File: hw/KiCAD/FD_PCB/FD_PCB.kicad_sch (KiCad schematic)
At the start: 120 parts, among them J1 Barrel_Jack_Switch, J10 MQ-138 Gas Sensor, J11 KY-026 Flame Sensor, J12 MiCS-6814, J13 Conn_01x02, J14 HDC3022, J2 Conn_02x12_Odd_Even, J3 Conn_02x12_Odd_Even, J4 Conn_02x20_Odd_Even, J5 Conn_02x09_Odd_Even, J6 Conn_01x02, J7 Conn_02x09_Odd_Even, J8 MQ-4 Gas Sensor, J9 MQ-7 Gas Sensor, M1 Motor_Servo, M2 Motor_Servo, SW1 SW_Push, SW2 SW_Push, SW3 SW_Push, U1 Adafruit ST7735R, U2 MAX98357A, U3 ADS1115IDGS, U4 ADS1115IDGS, U5 Winsen ZE07-CO Module

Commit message: update kicad stuff
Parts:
- removed D5: Red LED, ECE445L:LED_D5.0mm, symbol ECE445L:LED
- removed D6: Green LED, ECE445L:LED_D5.0mm, symbol ECE445L:LED
- removed J5, J7: Conn_02x09_Odd_Even, symbol Connector_Generic:Conn_02x09_Odd_Even
- removed R3: 2k, symbol Device:R_US
- removed R4: 1k, symbol Device:R_US
- removed TP10: TestPoint, symbol Connector:TestPoint
- added J16, J7: Conn_01x08, symbol Connector_Generic:Conn_01x08
- added J5, J8: Conn_02x10_Odd_Even, symbol Connector_Generic:Conn_02x10_Odd_Even
- added TP1: TestPoint, symbol Connector:TestPoint
- renumbered J9 to J10, J10 to J11, J11 to J12, J12 to J13, J13 to J14, J14 to J15, J8 to J9, R12 to R10, R13 to R11, R14 to R12, R15 to R13, R16 to R14, R17 to R15, R18 to R16, R19 to R17, R20 to R18, R21 to R19, R22 to R20, R23 to R21, R24 to R22, R25 to R23, R26 to R24, R27 to R25, R28 to R26, R29 to R27, R30 to R28, R31 to R29, R5 to R3, R7 to R4, R9 to R5, R8 to R7, R10 to R8, R11 to R9, TP9 to TP10, TP15 to TP11, TP11 to TP12, TP12 to TP13, TP13 to TP14, TP7 to TP15, TP1 to TP2, TP2 to TP3, TP3 to TP4, TP4 to TP5, TP5 to TP6, TP6 to TP7, TP14 to TP8, TP8 to TP9
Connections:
- net +3V3: now also J2.5 (Pin_5), J5.7 (Pin_7), J5.9 (Pin_9); no longer D2.2 (A)
- net +5V: now also J5.1 (Pin_1), J5.3 (Pin_3), J5.5 (Pin_5); no longer D1.2 (A)
- net GND: now also J5.10 (Pin_10), J5.12 (Pin_12), J5.14 (Pin_14), J5.16 (Pin_16), J5.18 (Pin_18), J5.2 (Pin_2), J5.20 (Pin_20), J5.4 (Pin_4), J5.6 (Pin_6), J5.8 (Pin_8)
- net GPIO01: now also J2.15 (Pin_15); no longer J2.13 (Pin_13)
- net GPIO09: now also J2.19 (Pin_19); no longer J2.17 (Pin_17)
- net GPIO11: now also J2.17 (Pin_17); no longer J2.15 (Pin_15)
- net GPIO12: now also J5.19 (Pin_19); no longer J2.23 (Pin_23)
- net I2C1_SCL: now also J5.15 (Pin_15)
- net I2C1_SDA: now also J5.17 (Pin_17)
- net SB_+3V3: now also R7.1, J7.3 (Pin_3), J8.7 (Pin_7), J8.9 (Pin_9)
- net SB_+5V: now also J7.1 (Pin_1), J8.1 (Pin_1), J8.3 (Pin_3), J8.5 (Pin_5)
- net SB_GND: now also R6.1, J8.10 (Pin_10), J8.12 (Pin_12), J8.14 (Pin_14), J8.16 (Pin_16), J8.18 (Pin_18), J8.2 (Pin_2), J8.20 (Pin_20), J8.4 (Pin_4), J8.6 (Pin_6), J8.8 (Pin_8)
- net SB_I2C1_SCL: now also J8.15 (Pin_15)
- net SB_I2C1_SDA: now also J8.17 (Pin_17)
- net SB_UART1_RXD: now also J8.13 (Pin_13)
- net SB_UART1_TXD: now also J8.11 (Pin_11)
- net SPI0_CS0: now also J2.13 (Pin_13); no longer J2.11 (Pin_11)
- net SPI0_MISO: now also J2.9 (Pin_9); no longer J2.7 (Pin_7)
- net SPI0_MOSI: now also J2.11 (Pin_11); no longer J2.9 (Pin_9)
- net SPI0_SCK: now also J2.7 (Pin_7); no longer J2.5 (Pin_5)
- net SPI1_CS1: now also J2.23 (Pin_23); no longer J2.19 (Pin_19)
- net UART1_RXD: now also J5.13 (Pin_13)
- net UART1_TXD: now also J5.11 (Pin_11)
- net UI_+3V3: now also J3.5 (Pin_5), TP1.1; no longer R7.1
- net UI_GND: no longer R6.1
- net UI_GPIO01: now also J3.15 (Pin_15); no longer J3.13 (Pin_13)
- net UI_GPIO09: now also J3.19 (Pin_19); no longer J3.17 (Pin_17)
- net UI_GPIO11: now also J3.17 (Pin_17); no longer J3.15 (Pin_15)
- net UI_SPI0_CS0: now also J3.13 (Pin_13); no longer J3.11 (Pin_11)
- net UI_SPI0_MISO: now also J3.9 (Pin_9); no longer J3.7 (Pin_7)
- net UI_SPI0_MOSI: now also J3.11 (Pin_11); no longer J3.9 (Pin_9)
- net UI_SPI0_SCK: now also J3.7 (Pin_7); no longer J3.5 (Pin_5)
- net UI_SPI1_CS1: now also J3.23 (Pin_23), TP3.1; no longer J3.19 (Pin_19), TP15.1
- net LED_RED-: now reaches R8.2
- net LED_RED-: now also J7.2 (Pin_2)
- net at D2.1 (K): now also J16.4 (Pin_4)
- net LED_GREEN-: now reaches R9.2
- net LED_GREEN-: now also J7.4 (Pin_4)
- net at D4.1 (K): now also J16.8 (Pin_8); no longer R6.2
- net at D1.1 (K): now also J16.2 (Pin_2)
- net at D3.2 (A): now also J16.5 (Pin_5); no longer R7.2
- removed net UI_GPIO12: D3.1 (K), D4.2 (A), J3.23 (Pin_23), TP3.1
- new net: D1.2 (A), J16.1 (Pin_1)
- new net: D4.2 (A), J16.7 (Pin_7)
- new net: D2.2 (A), J16.3 (Pin_3)
- new net: D3.1 (K), J16.6 (Pin_6)
- new net LED_BLUE+: J7.5 (Pin_5), R7.2
- new net LED_BLUE-: J7.6 (Pin_6), J7.7 (Pin_7), J8.19 (Pin_19), TP15.1
- new net LED_YELLOW-: J7.8 (Pin_8), R6.2
- no-connect marks 28 -> 27
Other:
- note added: "20-Trace Ribbon Cable"
- note added: "LED BOARD"
- note added: "LED BOARD CONN"
- note removed: "18-Trace Ribbon Cable"
- moved on the sheet: R5, R6, R7, R9, SW3, TP11, TP12, TP13, TP14, TP15, TP8

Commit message: Finish schematic and start on PCB design. Much progress.
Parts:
- removed C1, C2, C3, C4: C, ECE445L:C_Axial_200mil, symbol ECE445L:C
- removed FB1, FB2: FerriteBead, symbol Device:FerriteBead
- removed R3, R4: 100k, symbol Device:R_US
- removed TP11, TP6, TP7: TestPoint, symbol Connector:TestPoint
- removed U1: Adafruit ST7735R, ECE445L:adafruit_st7735r2, symbol ECE445L:Adafruit_ST7735R
- removed U2: MAX98357A, Package_DFN_QFN:TQFN-16-1EP_3x3mm_P0.5mm_EP1.23x1.23mm, symbol MichaelECEPartsCustom:MAX98357A-Modified
- removed U5: Winsen ZE07-CO Module, symbol MichaelECEPartsCustom:ZE07-CO
- added C1, C2, C3: 220u, ECE445L:CP_Radial_Tantal200mil, symbol ECE445L:C_Polarized
- added C10, C11, C12, C15: 1u, Capacitor_SMD:C_0805_2012Metric, symbol ECE445L:C
- added C16: 10u, ECE445L:C_Axial_200mil, symbol ECE445L:C
- added C17, C18, C19, C20: 0.1u, Capacitor_SMD:C_0805_2012Metric, symbol ECE445L:C
- added C21, C4, C5: 4.7u, ECE445L:CP_Radial_Tantal200mil, symbol ECE445L:C_Polarized
- added C6, C9: 47u, ECE445L:CP_Radial_Tantal200mil, symbol ECE445L:C_Polarized
- added D5: +5V PWR, ECE445L:LED_D5.0mm, symbol ECE445L:LED
- added D6: +3V3 PWR, ECE445L:LED_D5.0mm, symbol ECE445L:LED
- added J10, J11, J7: Conn_01x02, Connector_PinHeader_2.54mm:PinHeader_1x02_P2.54mm_Vertical, symbol Connector_Generic:Conn_01x02
- added J18: Conn_01x10, Connector_PinHeader_2.00mm:PinHeader_1x10_P2.00mm_Vertical, symbol Connector_Generic:Conn_01x10
- added J19: Conn_01x05, Connector_PinHeader_2.00mm:PinHeader_1x05_P2.00mm_Vertical, symbol Connector_Generic:Conn_01x05
- added J6: Conn_01x07, Connector_PinHeader_2.54mm:PinHeader_1x07_P2.54mm_Vertical, symbol Connector_Generic:Conn_01x07
- added J9: Conn_01x16, Connector_PinHeader_2.54mm:PinHeader_1x16_P2.54mm_Vertical, symbol Connector_Generic:Conn_01x16
- added R19: 560k, Resistor_SMD:R_0805_2012Metric, symbol Device:R_US
- added R2: 100k, Resistor_SMD:R_0805_2012Metric, symbol Device:R_US
- added R20: 150k, Resistor_SMD:R_0805_2012Metric, symbol Device:R_US
- added R21: 15k, Resistor_SMD:R_0805_2012Metric, symbol Device:R_US
- added R32, R33: 0, Resistor_SMD:R_0805_2012Metric, symbol Device:R_US
- added R34: 2k, Resistor_SMD:R_0805_2012Metric, symbol Device:R_US
- added R35: 1k, Resistor_SMD:R_0805_2012Metric, symbol Device:R_US
- added TP46, TP5, TP8: TestPoint, TestPoint:TestPoint_Loop_D3.50mm_Drill1.4mm_Beaded, symbol Connector:TestPoint
- added U2, U3: OPA2350, ECE445L:DIP-8_W7.62mm_LongPads, symbol ECE445L:OPA2350
- C13: renamed from C6; footprint ECE445L:C_Axial_200mil -> Capacitor_SMD:C_0805_2012Metric
- C14: renamed from C8; footprint ECE445L:C_Axial_200mil -> Capacitor_SMD:C_0805_2012Metric
- C7: renamed from C5; footprint ECE445L:C_Axial_200mil -> Capacitor_SMD:C_0805_2012Metric
- C8: renamed from C7; footprint ECE445L:C_Axial_200mil -> Capacitor_SMD:C_0805_2012Metric
- FB1: renamed from FB3; footprint (none) -> Resistor_SMD:R_0603_1608Metric
- FB2: renamed from FB5; footprint (none) -> Resistor_SMD:R_0603_1608Metric
- FB3: renamed from FB4; footprint (none) -> Resistor_SMD:R_0603_1608Metric
- FB4: renamed from FB6; footprint (none) -> Resistor_SMD:R_0603_1608Metric
- J1: footprint (none) -> Connector_BarrelJack:BarrelJack_Wuerth_6941xx301002
- J12: renamed from J6; footprint (none) -> Connector_JST:JST_PH_B2B-PH-K_1x02_P2.00mm_Vertical
- J13: renamed from J8; footprint (none) -> Connector_PinHeader_2.54mm:PinHeader_2x10_P2.54mm_Vertical
- J14: renamed from J9; footprint (none) -> Connector_PinHeader_2.54mm:PinHeader_1x04_P2.54mm_Vertical
- J15: renamed from J10; footprint (none) -> Connector_PinHeader_2.54mm:PinHeader_1x04_P2.54mm_Vertical
- J16: renamed from J11; footprint (none) -> Connector_PinHeader_2.54mm:PinHeader_1x04_P2.54mm_Vertical
- J17: renamed from J12; footprint (none) -> Connector_PinHeader_2.54mm:PinHeader_1x04_P2.54mm_Vertical
- J2, J3: footprint (none) -> Connector_PinHeader_2.54mm:PinHeader_2x12_P2.54mm_Vertical
- J20: renamed from J15; footprint (none) -> Connector_PinHeader_2.54mm:PinHeader_1x06_P2.54mm_Vertical
- J21: renamed from J16; footprint (none) -> Connector_PinHeader_2.54mm:PinHeader_1x08_P2.54mm_Vertical
- J22: renamed from J13; footprint (none) -> Connector_PinHeader_2.54mm:PinHeader_1x05_P2.54mm_Vertical
- J23: renamed from J14; footprint (none) -> Connector_PinHeader_2.54mm:PinHeader_1x02_P2.54mm_Vertical
- J4: footprint (none) -> Connector_PinHeader_2.54mm:PinHeader_2x20_P2.54mm_Vertical
- J5: footprint (none) -> Connector_PinHeader_2.54mm:PinHeader_2x10_P2.54mm_Vertical
- J8: renamed from J7; footprint (none) -> Connector_PinHeader_2.54mm:PinHeader_1x08_P2.54mm_Vertical
- M1, M2: footprint (none) -> Connector_PinHeader_2.54mm:PinHeader_1x03_P2.54mm_Vertical
- R1: footprint (none) -> Resistor_SMD:R_0805_2012Metric
- R10: renamed from R11; footprint (none) -> Resistor_SMD:R_0805_2012Metric
- R11: renamed from R12; footprint (none) -> Resistor_SMD:R_0805_2012Metric
- R12: renamed from R16; footprint (none) -> Resistor_SMD:R_0805_2012Metric
- R13: renamed from R17; footprint (none) -> Resistor_SMD:R_0805_2012Metric
- R14: renamed from R18; footprint (none) -> Resistor_SMD:R_0805_2012Metric
- R15: renamed from R22; footprint (none) -> Resistor_SMD:R_0805_2012Metric
- R16: renamed from R24; footprint (none) -> Resistor_SMD:R_0805_2012Metric
- R17: renamed from R26; footprint (none) -> Resistor_SMD:R_0805_2012Metric
- R18: renamed from R28; footprint (none) -> Resistor_SMD:R_0805_2012Metric
- R22: renamed from R13; footprint (none) -> Resistor_SMD:R_0805_2012Metric
- R23: renamed from R14; footprint (none) -> Resistor_SMD:R_0805_2012Metric
- R24: renamed from R15; footprint (none) -> Resistor_SMD:R_0805_2012Metric
- R25: renamed from R19; footprint (none) -> Resistor_SMD:R_0805_2012Metric
- R26: renamed from R20; footprint (none) -> Resistor_SMD:R_0805_2012Metric
- R27: renamed from R21; footprint (none) -> Resistor_SMD:R_0805_2012Metric
- R28: renamed from R23; footprint (none) -> Resistor_SMD:R_0805_2012Metric
- R29: renamed from R25; footprint (none) -> Resistor_SMD:R_0805_2012Metric
- R3: renamed from R2; footprint (none) -> Resistor_SMD:R_0805_2012Metric
- R30: renamed from R27; footprint (none) -> Resistor_SMD:R_0805_2012Metric
- R31: renamed from R29; footprint (none) -> Resistor_SMD:R_0805_2012Metric
- R4: renamed from R5; footprint (none) -> Resistor_SMD:R_0805_2012Metric
- R5: renamed from R6; footprint (none) -> Resistor_SMD:R_0805_2012Metric
- R6: renamed from R7; footprint (none) -> Resistor_SMD:R_0805_2012Metric
- R7: renamed from R8; footprint (none) -> Resistor_SMD:R_0805_2012Metric
- R8: renamed from R9; footprint (none) -> Resistor_SMD:R_0805_2012Metric
- R9: renamed from R10; footprint (none) -> Resistor_SMD:R_0805_2012Metric
- SW1, SW2, SW3: footprint (none) -> Button_Switch_THT:SW_PUSH_6mm
- TP1, TP10, TP12, TP13, TP14, TP15, TP16, TP17, TP18, TP19, TP2, TP20, TP21, TP22, TP23, TP24, TP25, TP26, TP27, TP28, TP29, TP3, TP30, TP31, TP32, TP33, TP34, TP35, TP36, TP37, TP38, TP39, TP4, TP40, TP41, TP42, TP45, TP9: footprint (none) -> TestPoint:TestPoint_Loop_D3.50mm_Drill1.4mm_Beaded
- TP43: renamed from TP44; footprint (none) -> TestPoint:TestPoint_Loop_D3.50mm_Drill1.4mm_Beaded
- TP44: renamed from TP43; footprint (none) -> TestPoint:TestPoint_Loop_D3.50mm_Drill1.4mm_Beaded
- TP6: renamed from TP5; footprint (none) -> TestPoint:TestPoint_Loop_D3.50mm_Drill1.4mm_Beaded
- TP7: renamed from TP8; footprint (none) -> TestPoint:TestPoint_Loop_D3.50mm_Drill1.4mm_Beaded
- renumbered U3 to U1
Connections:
- net +5V_EXT: now also C1.1, C16.1, C17.1, C18.1, C19.1, C2.1, C20.1, C3.1, C6.1, J10.1 (Pin_1), J6.1 (Pin_1), J7.1 (Pin_1)
- net Ain10: now also C10.1
- net Ain11: now also C11.1
- net Ain12: now also C12.1
- net GND: now also C1.2, C16.2, C17.2, C18.2, C19.2, C2.2, C20.2, C3.2, C6.2, J10.2 (Pin_2), J6.2 (Pin_2), J7.2 (Pin_2), R2.1, TP8.1
- net I2C1_SCL: now also J5.17 (Pin_17); no longer J5.15 (Pin_15)
- net I2C1_SDA: now also J5.15 (Pin_15); no longer J5.17 (Pin_17)
- net I2S0_DOUT: now also J6.5 (Pin_5)
- net I2S0_FS: now also J6.7 (Pin_7)
- net I2S0_SCK: now also J6.6 (Pin_6)
- net MiCS_CO: now also R24.2, U2.1, U2.2 (-); no longer J22.1 (Pin_1), R22.2
- net MiCS_NH3: now also U2.6 (-), U2.7; no longer J22.2 (Pin_2)
- net MiCS_NO2: now also R22.2, U3.1, U3.2 (-); no longer J22.3 (Pin_3), R24.2
- net SB_+3V3: now also C21.1, D6.2 (A)
- net SB_+5V: now also C15.2, C4.1, C5.1, C9.1, D5.2 (A), J18.1 (Pin_1), R19.1, R20.1, R21.1, U2.8 (V+), U3.8 (V+)
- net SB_GND: now also C10.2, C11.2, C12.2, C15.1, C21.2, C4.2, C5.2, C9.2, J18.2 (Pin_2), J19.5 (Pin_5), R33.1, R34.1, R35.1, U2.4 (V-), U3.4 (V-)
- net SB_I2C1_SCL: now also J13.17 (Pin_17); no longer J13.15 (Pin_15)
- net SB_I2C1_SDA: now also J13.15 (Pin_15); no longer J13.17 (Pin_17)
- net SB_UART1_RXD: now also J18.9 (Pin_9)
- net SB_UART1_TXD: now also J18.8 (Pin_8)
- net UI_+3V3: now also J9.15 (Pin_15), J9.2 (Pin_2)
- net UI_GND: now also TP9.1, J9.1 (Pin_1), J9.16 (Pin_16), TP46.1
- net UI_GPIO01: now also J9.6 (Pin_6)
- net UI_GPIO09: now also TP5.1
- net UI_GPIO11: now also J9.7 (Pin_7)
- net UI_SPI0_CS0: now also J9.10 (Pin_10)
- net UI_SPI0_MOSI: now also J9.8 (Pin_8)
- net UI_SPI0_SCK: now also J9.9 (Pin_9)
- net UI_SPI1_CS1: no longer TP9.1
- net ZE07-CO_DAC: now also J18.6 (Pin_6)
- net at J12.1 (Pin_1): now also J11.1 (Pin_1)
- net at J12.2 (Pin_2): now also J11.2 (Pin_2)
- new net: D5.1 (K), R34.2
- new net: J22.3 (Pin_3), R21.2, U3.3 (+)
- new net: J6.4 (Pin_4), R2.2
- new net: D6.1 (K), R35.2
- new net: J22.1 (Pin_1), R19.2, U2.3 (+)
- new net: J22.2 (Pin_2), R20.2, U2.5 (+)
- new net: R33.2, U3.5 (+)
- new net: R32.2, U3.6 (-)
- new net: R32.1, U3.7
- no-connect marks 27 -> 33
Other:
- note added: "MAX98357 Vout"
- note added: "MAX98357A Breakout"
- note added: "SEN0219 PWR"
- note added: "ST7735R LCD"
- note added: "Winsen ZE07-CO Module"
- moved on the sheet: C13, C14, FB3, FB4, J12, J22, J23, R22, R23, R24, R25, R26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

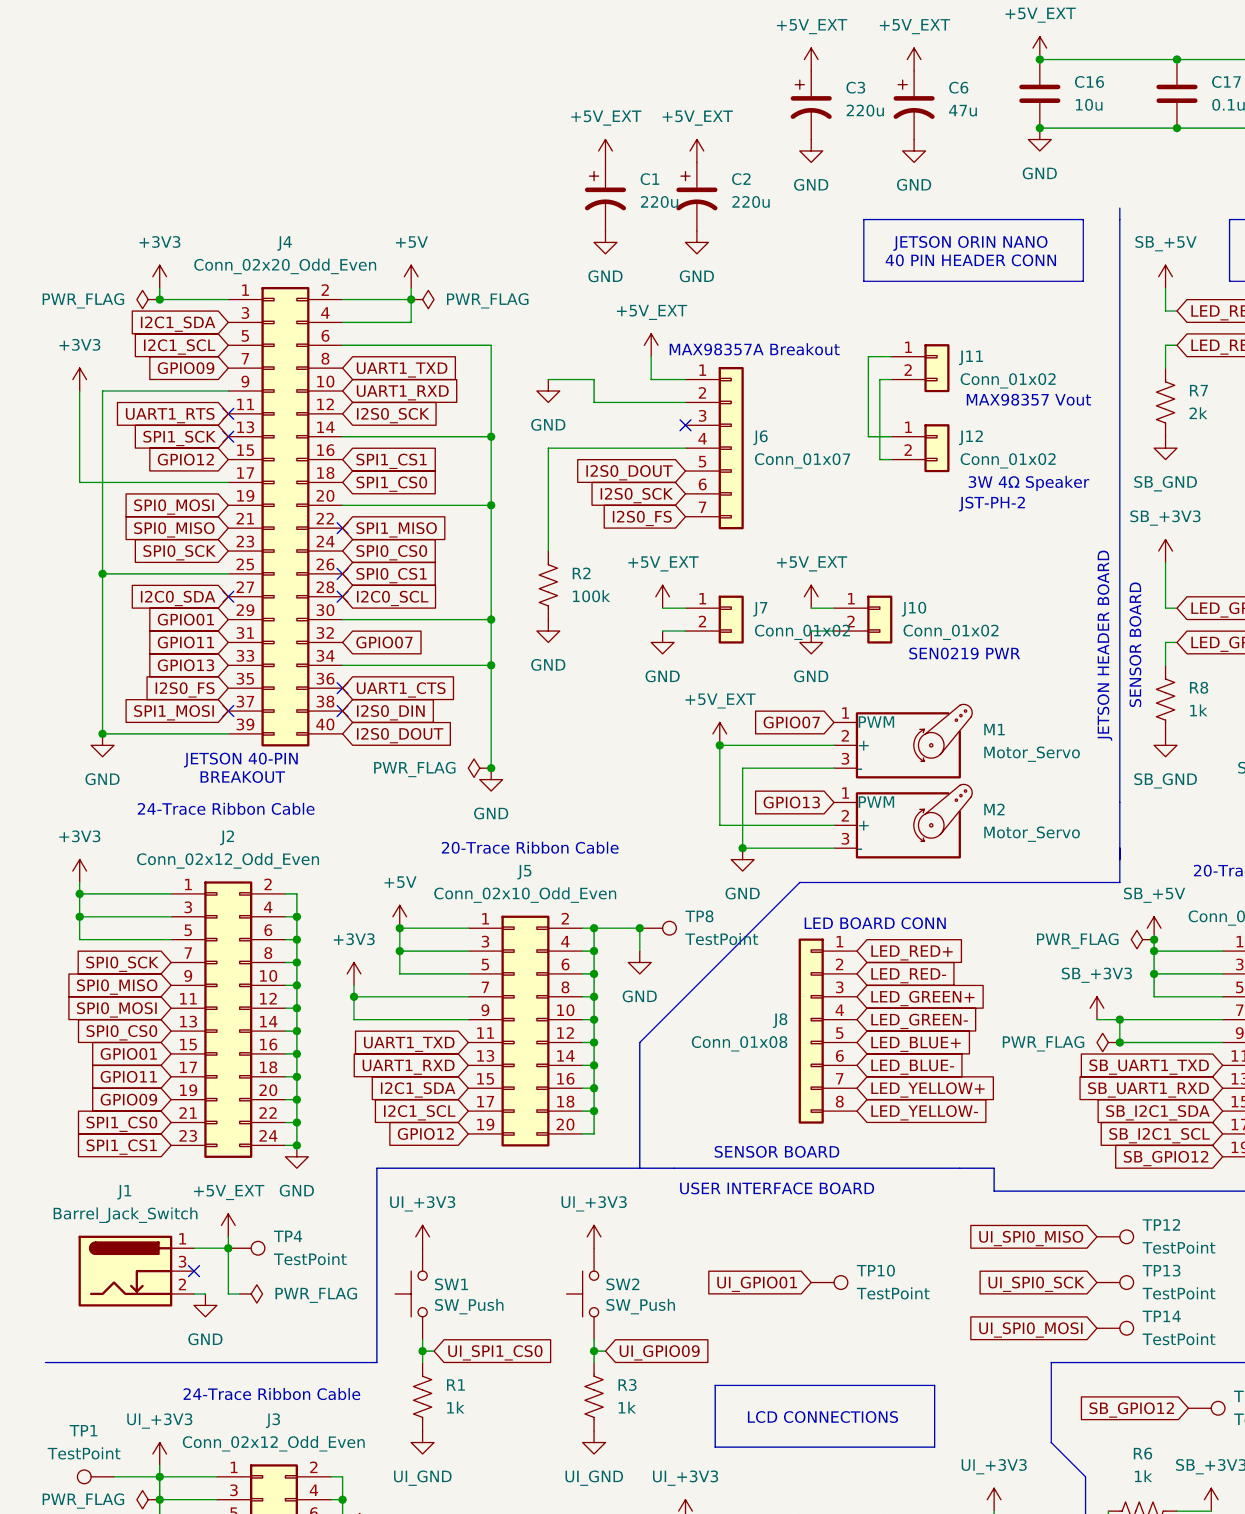
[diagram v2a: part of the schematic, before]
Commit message: finish sensor board, lcd board, led board, and header board
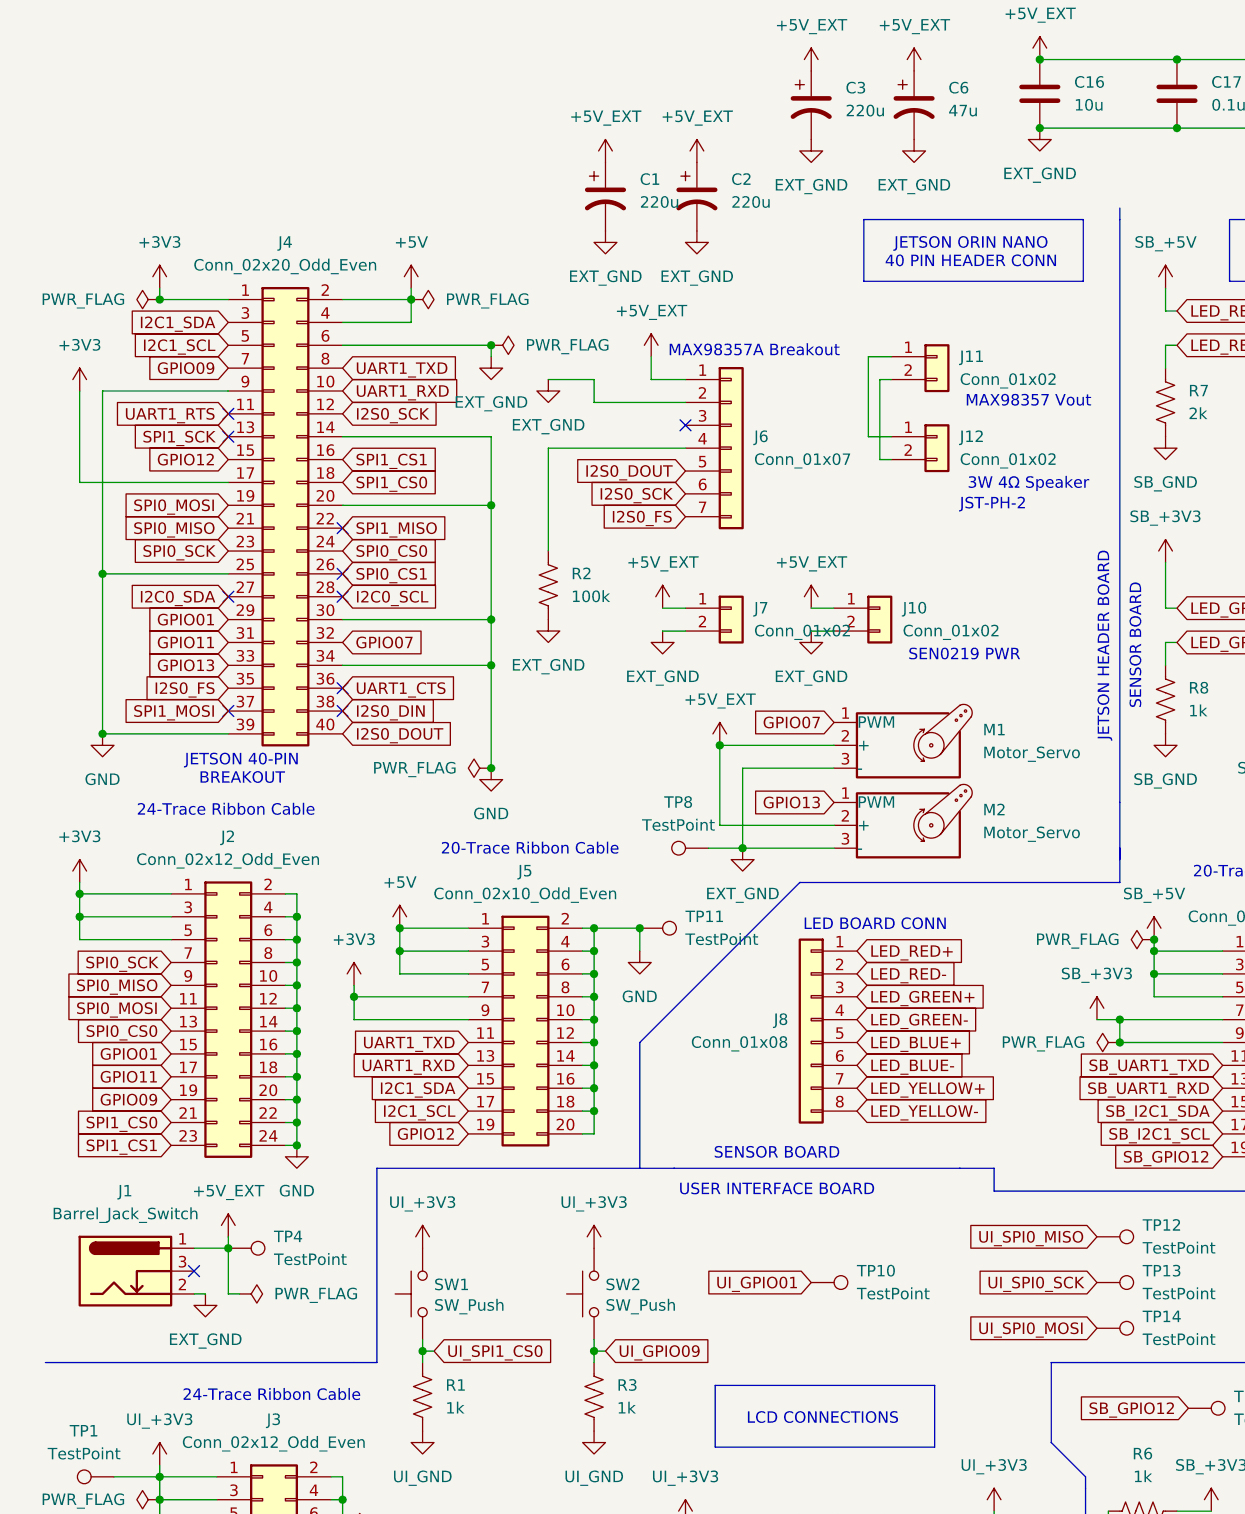
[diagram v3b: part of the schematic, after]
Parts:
- added TP11: TestPoint, TestPoint:TestPoint_Loop_D3.50mm_Drill1.4mm_Beaded, symbol Connector:TestPoint
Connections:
- net GND: now also TP11.1; no longer C1.2, C16.2, C17.2, C18.2, C19.2, C2.2, C20.2, C3.2, C6.2, J1.2, J10.2 (Pin_2), J4.6 (Pin_6), J6.2 (Pin_2), J7.2 (Pin_2), M1.3 (-), M2.3 (-), R2.1, TP8.1
- new net EXT_GND: C1.2, C16.2, C17.2, C18.2, C19.2, C2.2, C20.2, C3.2, C6.2, J1.2, J10.2 (Pin_2), J4.6 (Pin_6), J6.2 (Pin_2), J7.2 (Pin_2), M1.3 (-), M2.3 (-), R2.1, TP8.1
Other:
- moved on the sheet: TP8
